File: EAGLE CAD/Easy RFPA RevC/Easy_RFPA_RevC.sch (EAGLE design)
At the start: 286 parts, among them IC1 LM741D, IC2 LM741D, IC3 LM393D, IC5 74AHC1G00DBV, IC6 74LS74D, IC7 74AHC1G86DBV, J401 HDR_2X1282836-1282836-1, J402 KK_PCFAN, Q1 IRF630, Q101 IRF520N, Q102 IRF630, Q2 MOSFET_NBSS123SOT23, Q201 IRF630, Q202 IRF630, Q3 NPNMMBT3904SOT23_BEC, Q301 MOSFET_NBSS123SOT23, Q302 PNPSOT23_BEC, Q303 NPNMMBT3904SOT23_BEC, Q4 PNPSOT23_BEC, SW1 SPST_NO_TACT_RA43125608371643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, SW2 SPST_NO_TACT_RA43125608371643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, T1 HP1_TRAFO, T102 HP4_TRAFO, U1 OPAMP_QUADTLV274IDSOIC14, U302 OPAMP_QUADTLV274IDSOIC14, U401 LDO_3TERMMC78M12CTGTO220_VERT, U402 LDO_3TERMMC78M05CTGTO220_VERT, X1 1-227161-0, X2 1-227161-0, X4 1-227161-0, X402 HEATSINK_OMNI_DUALOMNI-UNI-30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

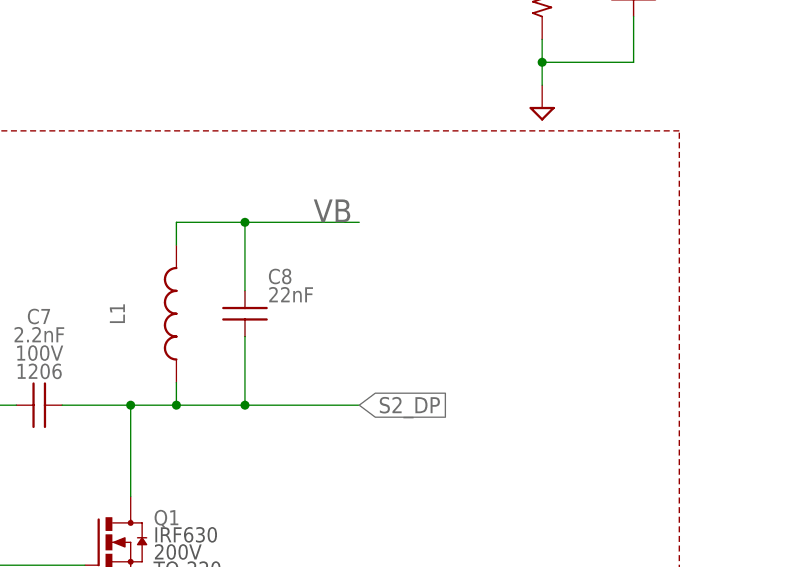
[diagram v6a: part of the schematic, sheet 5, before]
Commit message: Add bypass cap for VB near S2 bias Add 40mm wide heatsink to library adjust some trace widths
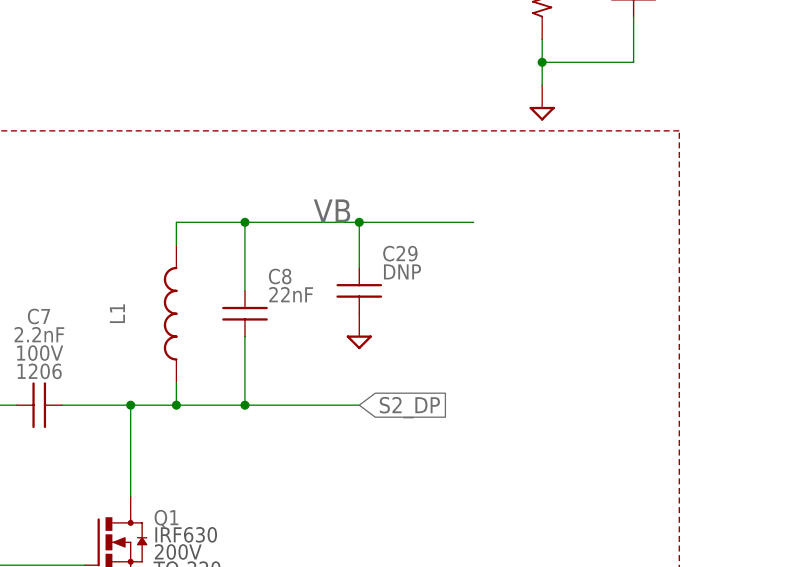
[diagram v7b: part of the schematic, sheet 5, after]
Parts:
- added C29: DNP, MDT_C:CGENC1812
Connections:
- net GND: now also C29.2
- net VB: now also C29.1
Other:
- note added: "One stage LC filter First stage is L1 and C1 Damping is with R and C2 in parallel with C1 C2=4*C1 f0=1/(w*pi*sqrt(L1*C1)) Z0=R=sqrt(L1/C1)) Two stage LC filter First stage is L1 and C1 Second stage is L2 and C2 Where L2=6*L1 and C2=4*C1 And L2 is shunted by R=sqrt(L1/(4C1))=sqrt(L1/C2) f0=1/(w*pi*sqrt(6*L1*C1))=1/(w*pi*sqrt(L2*C1)) Z0=sqrt(L1/C1)"
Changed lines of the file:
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@@
 </part>
 <part name="R54" library="MDT_R" deviceset="R90" device="1206_IPC" technology="GEN" value="0"/>
+<part name="C29" library="MDT_C" deviceset="C" device="C1812" technology="GEN" value="DNP">
+<attribute name="BOM" value="EXCLUDE"/>
+<attribute name="VOLTAGE" value="100V"/>
+</part>
+<part name="SUPPLY52" library="supply2" deviceset="GND" device=""/>
 </parts>
 <sheets>
@@
 <text x="375.92" y="139.7" size="2.54" layer="94" align="center">Thermal pads and heatsink clips</text>
 <text x="327.66" y="27.94" size="3.81" layer="94" align="center-left">Power Entry</text>
+<text x="152.4" y="208.28" size="1.778" layer="91">One stage LC filter
+First stage is L1 and C1
+Damping is with R and C2 in parallel with C1
+C2=4*C1
+f0=1/(w*pi*sqrt(L1*C1))
+Z0=R=sqrt(L1/C1))
+Two stage LC filter
+First stage is L1 and C1
+Second stage is L2 and C2
+Where L2=6*L1 and C2=4*C1
+And L2 is shunted by R=sqrt(L1/(4C1))=sqrt(L1/C2)
+f0=1/(w*pi*sqrt(6*L1*C1))=1/(w*pi*sqrt(L2*C1))
+Z0=sqrt(L1/C1)
+</text>
 </plain>
 <instances>
@@
 <instance part="C8" gate="G$1" x="292.1" y="124.46"/>
 <instance part="L1" gate="G$1" x="284.48" y="124.46" rot="R90"/>
+<instance part="C29" gate="G$1" x="304.8" y="127"/>
+<instance part="SUPPLY52" gate="GND" x="304.8" y="121.92" smashed="yes"/>
 </instances>
 <busses>
@@
 <pinref part="SUPPLY45" gate="GND" pin="GND"/>
 </segment>
+<segment>
+<pinref part="C29" gate="G$1" pin="2"/>
+<pinref part="SUPPLY52" gate="GND" pin="GND"/>
+</segment>
 </net>
 <net name="N$60" class="0">
@@
 <label x="299.72" y="134.62" size="2.54" layer="95"/>
 <pinref part="C8" gate="G$1" pin="1"/>
-<wire x1="292.1" y1="134.62" x2="304.8" y2="134.62" width="0.1524" layer="91"/>
 <wire x1="292.1" y1="127" x2="292.1" y2="134.62" width="0.1524" layer="91"/>
 <junction x="292.1" y="134.62"/>
 <pinref part="L1" gate="G$1" pin="2"/>
+<wire x1="292.1" y1="134.62" x2="304.8" y2="134.62" width="0.1524" layer="91"/>
+<pinref part="C29" gate="G$1" pin="1"/>
+<wire x1="304.8" y1="134.62" x2="317.5" y2="134.62" width="0.1524" layer="91"/>
+<wire x1="304.8" y1="129.54" x2="304.8" y2="134.62" width="0.1524" layer="91"/>
+<junction x="304.8" y="134.62"/>
 </segment>
 </net>
